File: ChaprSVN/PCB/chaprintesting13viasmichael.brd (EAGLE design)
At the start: 68.6 x 55.6 mm, 30 parts, among them M2 RN42 Module, T1 3906, T2 3904

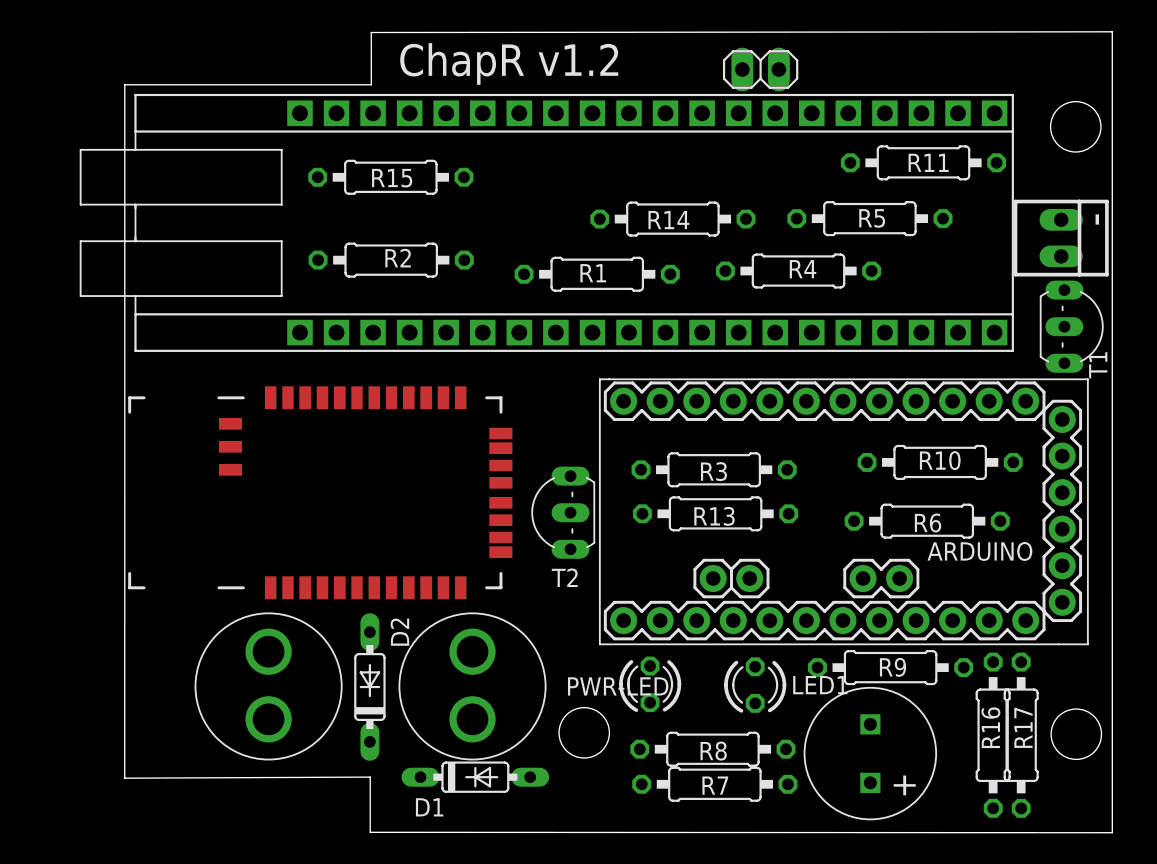
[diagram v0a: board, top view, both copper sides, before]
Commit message: 
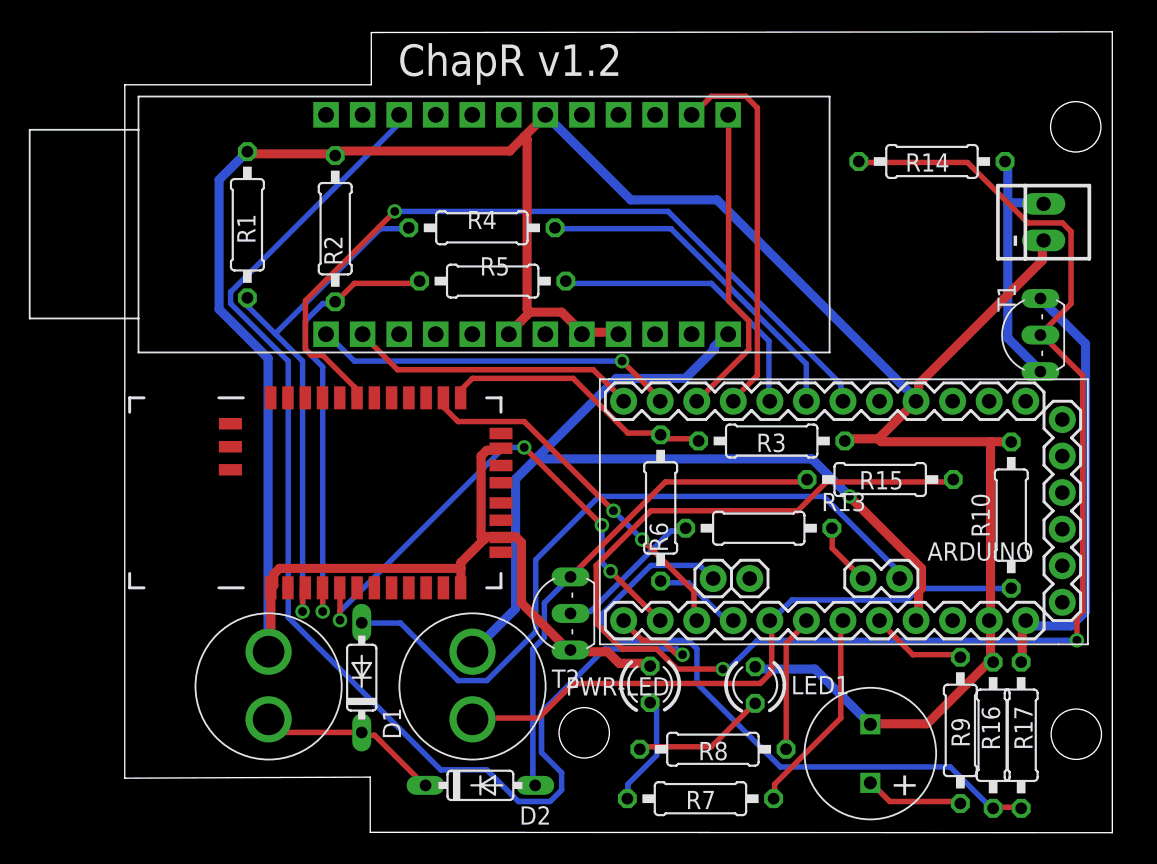
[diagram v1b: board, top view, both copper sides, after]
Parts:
- removed JP1: (no value), pinhead:1X02
- removed R11: 10k, resistor:0207/10
- removed U$3: VDIP2BIGHOLE, ChapR-Custom:VDIP2-BIGHOLE
- added V2DIP2: V2DIP2, ChapR-Custom:V2DIP2
- moved R15 40.0 mm to (54.5, 25.2)
- moved R5 26.6 mm to (27.6, 39.0)
- moved R1 24.5 mm to (10.6, 42.9), turned to 270 degrees
- moved R4 22.2 mm to (26.9, 42.7)
- moved R6 18.5 mm to (39.3, 23.2), turned to 270 degrees
- moved R14 18.4 mm to (58.1, 47.3)
- moved D1 10.5 mm to (18.5, 11.4), turned to 90 degrees
- moved D2 10.3 mm to (26.8, 3.92), turned to 0 degrees
- moved T2 7.00 mm to (31.7, 15.9)
- moved R9 6.52 mm to (60.1, 7.74), turned to 90 degrees
- moved R10 6.15 mm to (63.6, 22.7), turned to 270 degrees
- moved R3 4.47 mm to (47.0, 27.8)
- moved R2 4.46 mm to (16.7, 42.6), turned to 270 degrees
- moved T1 4.25 mm to (64.4, 35.2), turned to 90 degrees
- moved R13 3.16 mm to (46.1, 21.8)
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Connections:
- removed net LED1(BD5): U$3.4
- removed net LED2(BD6): U$3.5
- removed net N$22: JP1.1, M2.22, R11.2
- removed net NC(1): U$3.1
- removed net NC(2): U$3.40
- new net N$28: V2DIP2.P$24
- net +3V3: no longer JP1.2, U$3.32, U$3.38, U$3.39
- net +5V: now also V2DIP2.P$1; no longer U$3.2, U$3.3, U$3.9
- net GND: now also V2DIP2.P$18, V2DIP2.P$4, V2DIP2.P$5, V2DIP2.P$7; no longer R11.1, U$3.12, U$3.13, U$3.15, U$3.26
- net N$10: now also ARDUINO.D6, V2DIP2.P$14; no longer ARDUINO.D9, U$3.18
- net N$11: now also ARDUINO.D7, V2DIP2.P$13; no longer ARDUINO.D8, U$3.17
- net N$12: now also ARDUINO.D8, V2DIP2.P$12; no longer ARDUINO.D7, U$3.16
- net N$13: now also ARDUINO.D9, V2DIP2.P$11; no longer ARDUINO.D6, U$3.14
- net N$2: now also V2DIP2.P$22; no longer U$3.30
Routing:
- net GND: track 0.00 -> 228.4 mm
- net N$1: track 0.00 -> 114.4 mm, vias 0 -> 2
- net N$2: track 0.00 -> 88.9 mm, vias 0 -> 1
- net +5V: track 0.00 -> 66.0 mm, vias 0 -> 1
- net N$15: track 0.00 -> 54.7 mm, vias 0 -> 1
- net N$29: track 0.00 -> 49.9 mm
- net N$31: track 0.00 -> 46.3 mm
- net N$24: track 0.00 -> 43.4 mm
- net N$6: track 0.00 -> 37.5 mm, vias 0 -> 1
- net N$5: track 0.00 -> 36.3 mm, vias 0 -> 4
- net N$25: track 0.00 -> 35.0 mm
- net N$7: track 0.00 -> 31.4 mm, vias 0 -> 1
- net N$23: track 0.00 -> 30.8 mm
- net N$10: track 0.00 -> 26.5 mm
- net N$4: track 0.00 -> 25.5 mm, vias 0 -> 2
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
